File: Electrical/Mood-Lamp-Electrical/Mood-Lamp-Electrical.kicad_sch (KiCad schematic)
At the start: 3 parts, among them U1 ESP32C3

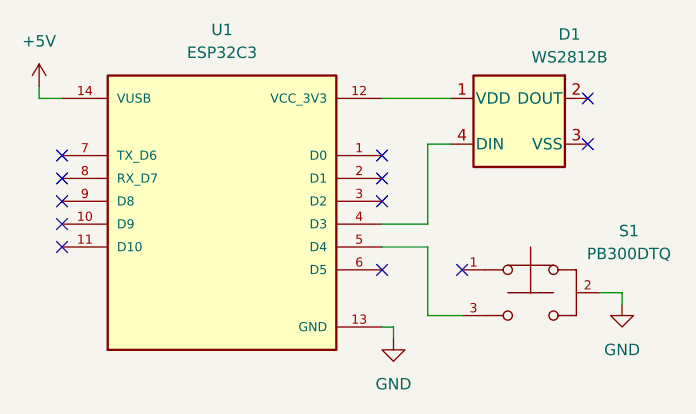
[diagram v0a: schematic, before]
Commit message: Updated moods and patterns
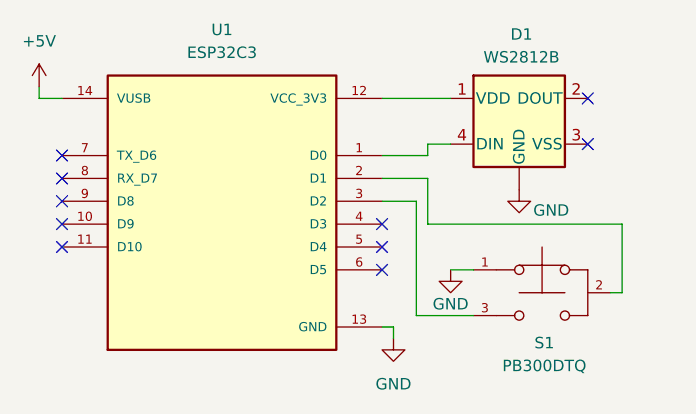
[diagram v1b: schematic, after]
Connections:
- net GND: now also D1. (GND), S1.1; no longer S1.2
- net at U1.1 (D0): now also D1.4 (DIN)
- net at U1.2 (D1): now also S1.2
- net at U1.3 (D2): now also S1.3
- net at U1.4 (D3): no longer D1.4 (DIN)
- net at U1.5 (D4): no longer S1.3
- no-connect marks 12 -> 10
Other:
- moved on the sheet: S1
